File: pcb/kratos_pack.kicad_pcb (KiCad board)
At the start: 4 copper layers, 44.2 x 20.2 mm, 116 parts, among them J1 USB_C_Receptacle_USB2.0, J2 PROG_CONN, J3 DBG_UART, J4 BAT_MID+NTC, J5 BAT_7.4V, J6 BAT_0V, J7 OUT+, J8 OUT-, Q1 AON7403, Q2 AON7414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

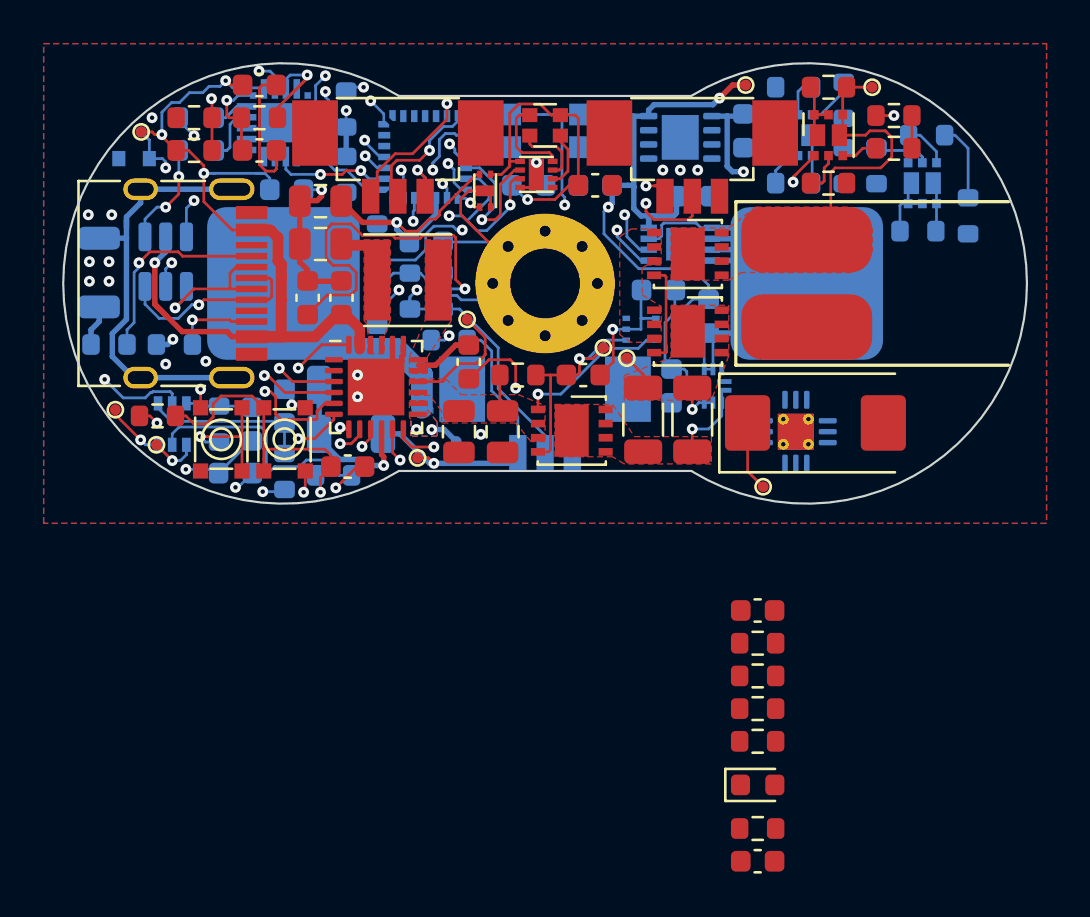
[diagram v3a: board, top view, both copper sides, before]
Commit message: PCB: route power and voltage measuring
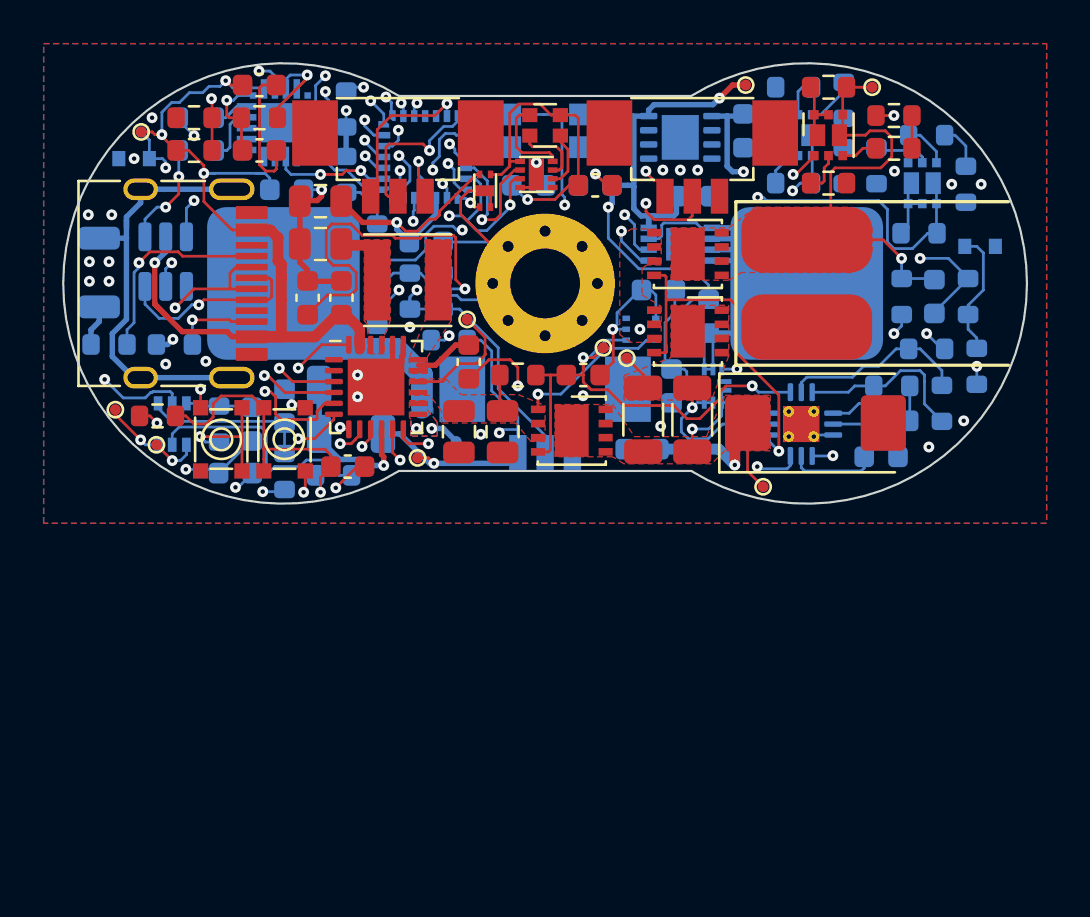
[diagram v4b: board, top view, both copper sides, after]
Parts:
- added D4: 3V3, Diode_SMD:D_SOD-523, B.Cu at (170.9, 98.3)
- added R41: 1k, Resistor_SMD:R_0603_1608Metric, B.Cu at (170.8, 103.8)
- added R42: 1k, Resistor_SMD:R_0603_1608Metric, B.Cu at (170.4, 100.6)
- C20, C23, D3, R25, R26, R27, R30, R32: moved to B.Cu
- moved C23 27.1 mm to (168.9, 100.6), turned to -90 degrees
- moved R32 25.3 mm to (167.4, 100.6), turned to -90 degrees
- moved R25 19.6 mm to (168.5, 103.0), turned to 180 degrees
- moved R26 16.4 mm to (169.2, 105.5), turned to -90 degrees
- moved D3 16.3 mm to (155.4, 107.6)
- moved R27 14.7 mm to (166.9, 104.7)
- moved R30 11.9 mm to (166.9, 106.3), turned to 180 degrees
- moved C20 9.04 mm to (166.4, 108.0)
- moved R4 1.45 mm to (170.3, 95.5)
- moved U8 0.43 mm to (162.8, 106.5)
- moved R34 0.11 mm to (168.2, 97.7)
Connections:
- J1 pad A8: no_connect_79 -> no_connect_78
- J1 pad B8: no_connect_80 -> no_connect_79
- Q4 pad 2: /B2_EN -> /ME_EN
- Q4 pad 3: /DIV_1 -> /DIV
- Q5 pad 2: /B1_EN -> /ME_EN
- Q5 pad 3: /DIV_2 -> /DIV_1
- Q6 pad 2: /OUT_EN -> /ME_EN
- Q6 pad 3: /DIV -> /DIV_2
- R16 pad 1: /DIV -> /DIV_2
- R3 pad 1: /DIV_1 -> /DIV
- R33 pad 1: /B2_EN -> /ME_EN
- R37 pad 1: /B1_EN -> /ME_EN
- R39 pad 1: /OUT_EN -> /ME_EN
- R8 pad 1: /DIV_2 -> /DIV_1
- U2 pad 1: no_connect_81 -> no_connect_80
- U2 pad 10: no_connect_102 -> no_connect_95
- U2 pad 11: no_connect_82 -> no_connect_81
- U2 pad 14: no_connect_83 -> no_connect_82
- U2 pad 15: no_connect_84 -> no_connect_83
- U2 pad 16: no_connect_85 -> no_connect_84
- U2 pad 19: no_connect_86 -> no_connect_85
- U2 pad 2: no_connect_87 -> no_connect_86
- U2 pad 20: no_connect_88 -> no_connect_87
- U3 pad 12: no_connect_89 -> /B2_MON
- U3 pad 13: no_connect_90 -> /B1_MON
- U3 pad 15: no_connect_91 -> /OUT_MON
- U3 pad 16: no_connect_92 -> /ME_EN
- U3 pad 17: no_connect_93 -> /CS_EN
- U3 pad 18: no_connect_94 -> no_connect_88
- U3 pad 19: no_connect_95 -> no_connect_89
- U3 pad 22: no_connect_96 -> no_connect_90
- U3 pad 24: no_connect_97 -> no_connect_91
- U3 pad 7: no_connect_98 -> /CS_MON
- U4 pad 1: no_connect_99 -> no_connect_92
- U5 pad 1: no_connect_100 -> no_connect_93
- U5 pad 2: no_connect_101 -> no_connect_94
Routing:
- net VCC: track 12.0 -> 54.9 mm, vias 2 -> 4
- net /B2_V: track 13.8 -> 47.4 mm, vias 2 -> 3
- net /B1_V: track 18.8 -> 40.5 mm, vias 1 -> 3
- net /CS_OUT: track 0.00 -> 14.3 mm, vias 0 -> 2
- net /UVLO: track 10.5 -> 22.5 mm, vias 1 -> 2
- net Net-(Q2-Pad4): track 4.89 -> 16.6 mm, vias 0 -> 1
- net Net-(Q2-Pad1): track 0.00 -> 11.7 mm, vias 0 -> 2
- net GND: track 109.2 -> 120.0 mm, vias 30 -> 41
- net Net-(R32-Pad2): track 0.00 -> 8.74 mm, vias 0 -> 2
- net Net-(R25-Pad2): track 0.00 -> 8.62 mm
- net Net-(R26-Pad2): track 0.00 -> 7.96 mm
- net /ME_EN: track 0.00 -> 7.77 mm, vias 0 -> 1
- net /CS_MON: track 0.00 -> 7.23 mm, vias 0 -> 1
- net /OUT_V: track 14.3 -> 21.4 mm, vias 0 -> 1
- net /SENSE: track 3.74 -> 9.39 mm
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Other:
- board text added: "TODO - connections for voltage measurement - conector polarity marking (silkscreen) - version number - Github link"

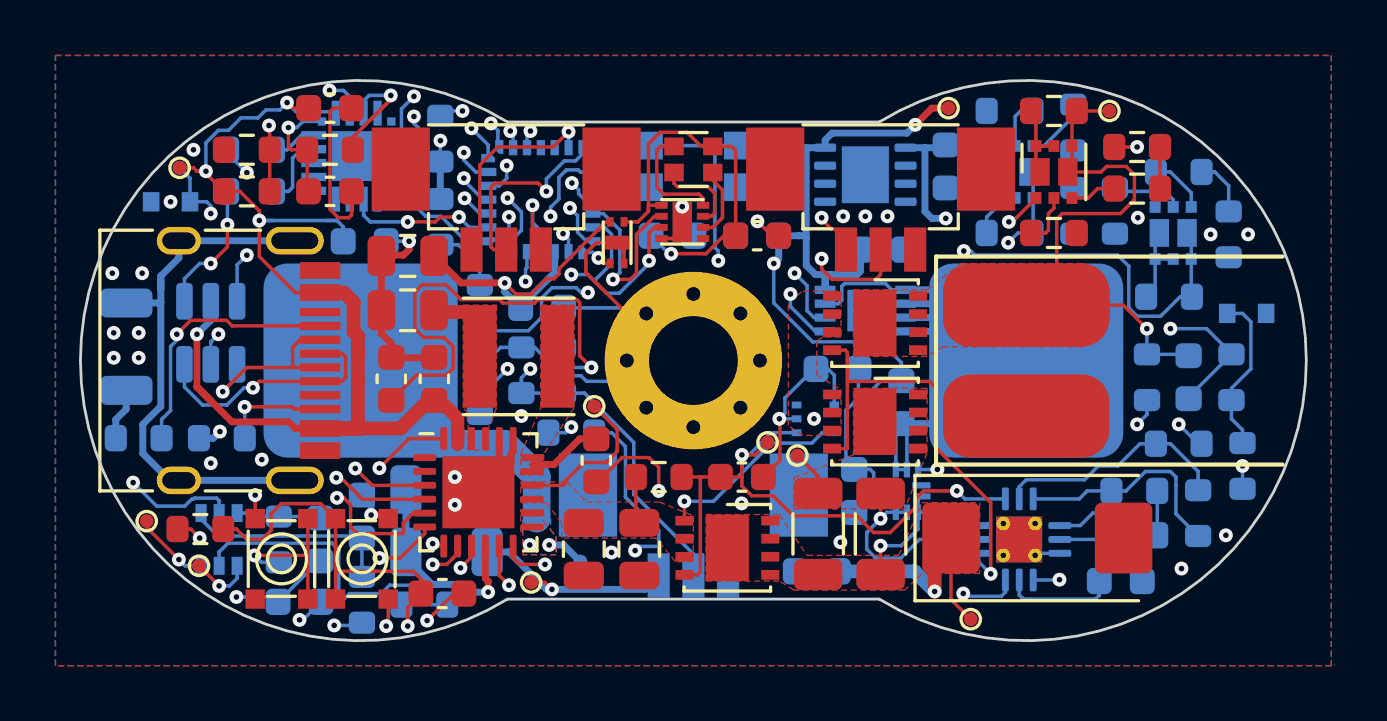
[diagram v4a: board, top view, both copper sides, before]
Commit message: PCB: finalization of routing, add silk screen
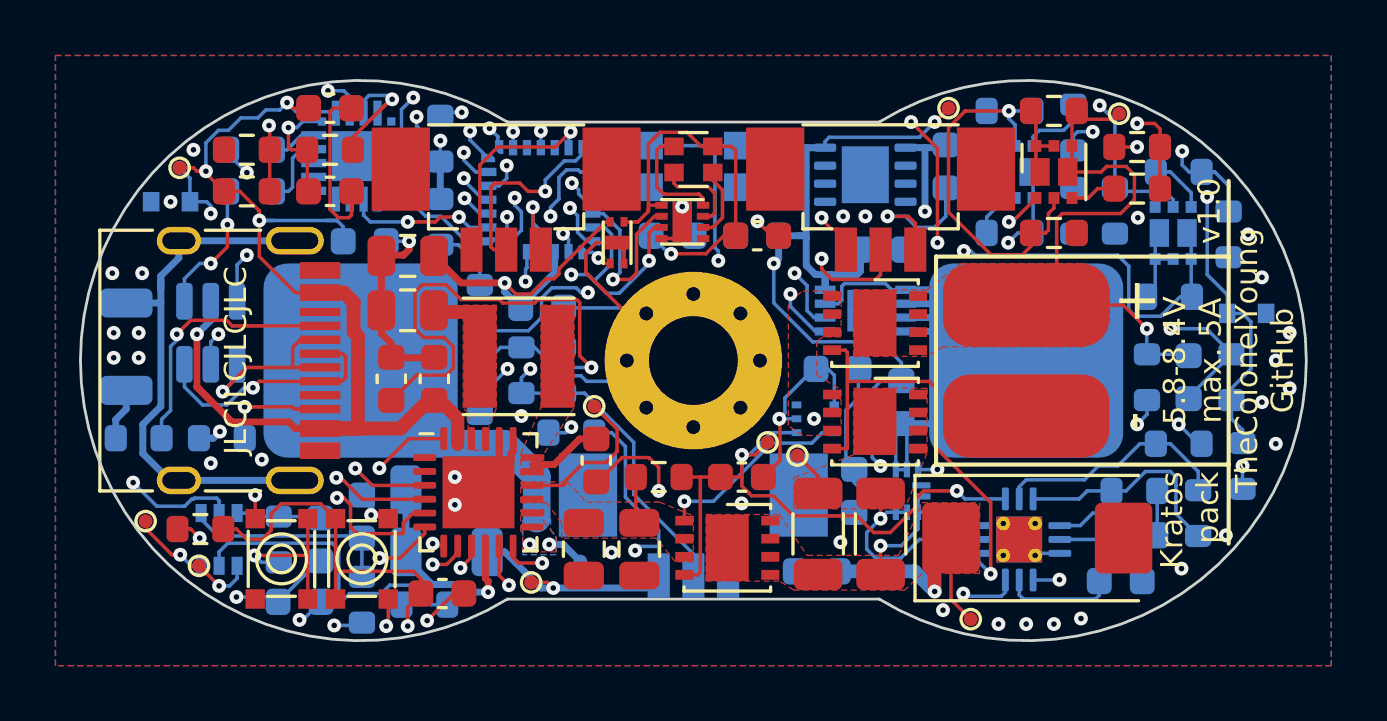
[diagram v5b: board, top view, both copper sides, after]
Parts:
- moved TP9 0.36 mm to (166.3, 91.1)
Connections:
- Q4 pad 3: /DIV -> /DIV_1
- Q5 pad 3: /DIV_1 -> /DIV_2
- Q6 pad 3: /DIV_2 -> /DIV
- R16 pad 1: /DIV_2 -> /DIV
- R3 pad 1: /DIV -> /DIV_1
- R8 pad 1: /DIV_1 -> /DIV_2
- U3 pad 17: /CS_EN -> no_connect_88
- U3 pad 18: no_connect_88 -> /CS_EN
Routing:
- net /ME_EN: track 7.77 -> 43.2 mm, vias 1 -> 3
- net /CS_MON: track 7.23 -> 39.0 mm, vias 1 -> 2
- net /CS_EN: track 0.65 -> 30.1 mm, vias 1 -> 4
- net /B2_MON: track 3.32 -> 29.5 mm, vias 1 -> 2
- net /OUT_MON: track 4.48 -> 28.9 mm, vias 1 -> 2
- net /B1_MON: track 2.70 -> 27.0 mm, vias 1 -> 2
- net GND: track 120.0 -> 131.5 mm, vias 41 -> 51
- net /DIV_2: track 1.68 -> 2.60 mm
- net /OUT_V: track 21.4 -> 22.0 mm
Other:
- board text added: "+"
- board text added: "-"
- board text added: "5.8-8.4V max. 5A"
- board text added: "JLCJLCJLCJLC"
- board text added: "Kratos pack"
- board text added: "TheColonelYoung GitHub"
- board text added: "v1.0"

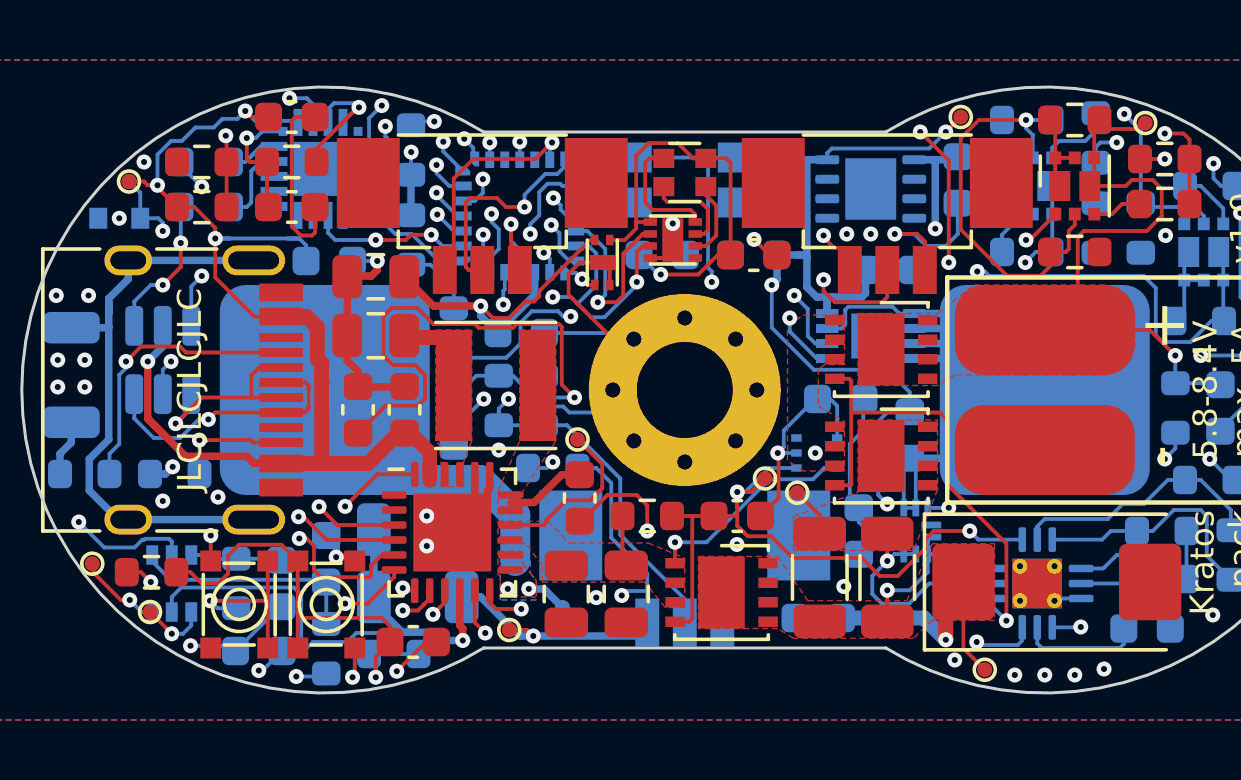
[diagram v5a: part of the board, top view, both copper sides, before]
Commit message: PCB: fix clearance based on JLCPCB capabilities
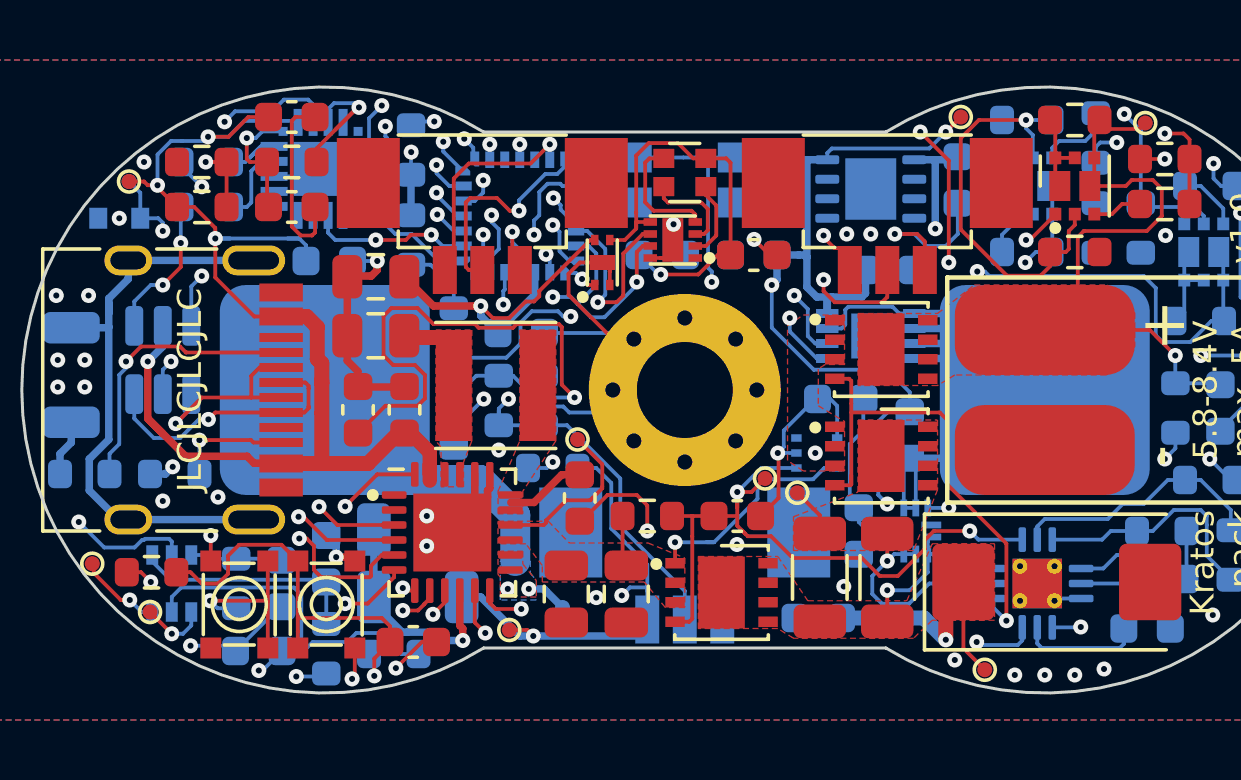
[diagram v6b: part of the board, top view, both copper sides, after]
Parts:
- moved J4 0.10 mm to (151.0, 106.9)
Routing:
- net VBUS: track 52.7 -> 53.9 mm
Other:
- board text removed: "TODO - connections for voltage measurement - conector polarity marking (silkscreen) - version number - Github link"

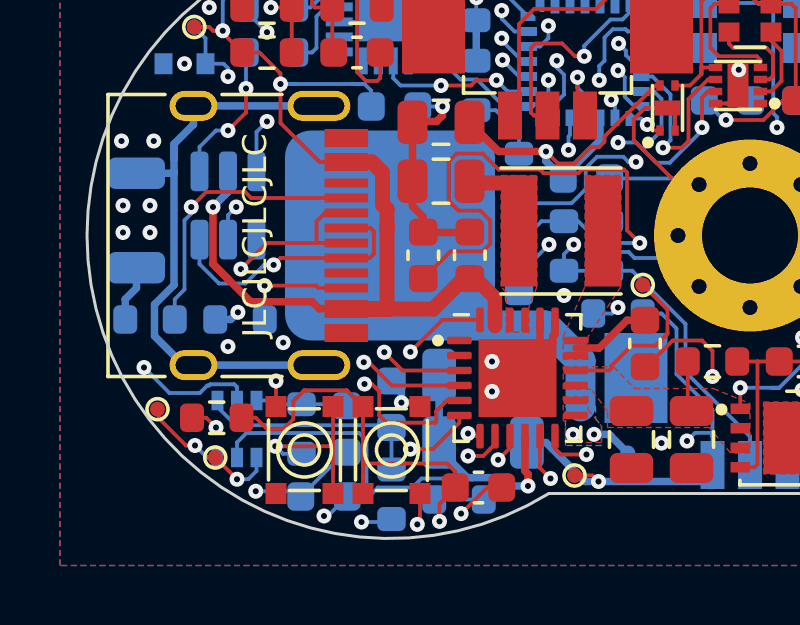
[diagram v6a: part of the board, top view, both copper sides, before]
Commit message: PCB: add 3D packages to parts
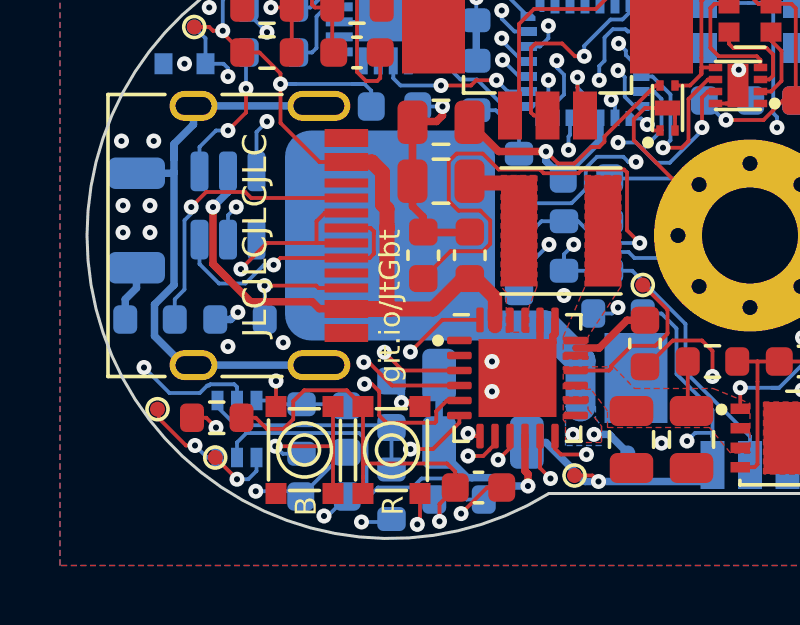
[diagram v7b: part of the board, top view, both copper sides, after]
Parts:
- added G***: LOGO, LOGO, B.Cu at (159.2, 107.3)
- added G***: LOGO, LOGO, B.Cu at (145.1, 105.3)
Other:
- board text added: "B"
- board text added: "R"
- board text added: "git.io/JtGbt"
